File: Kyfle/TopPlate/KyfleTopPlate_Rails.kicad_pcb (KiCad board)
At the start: 2 copper layers, 164 x 146.3 mm, 28 parts, among them SW2 KEY_SWITCH, SW2 PRO MICRO

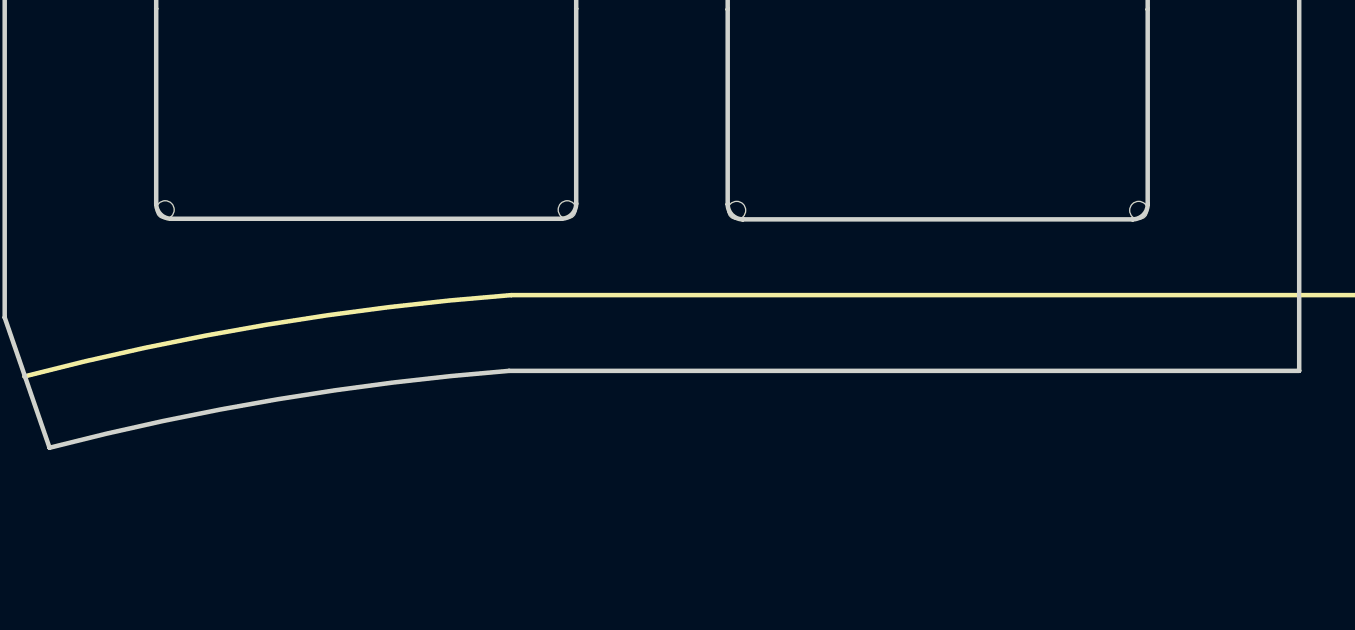
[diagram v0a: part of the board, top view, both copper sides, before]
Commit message: Found a solution to hold slightly better the middle "tongue" of board in the top plate with rails
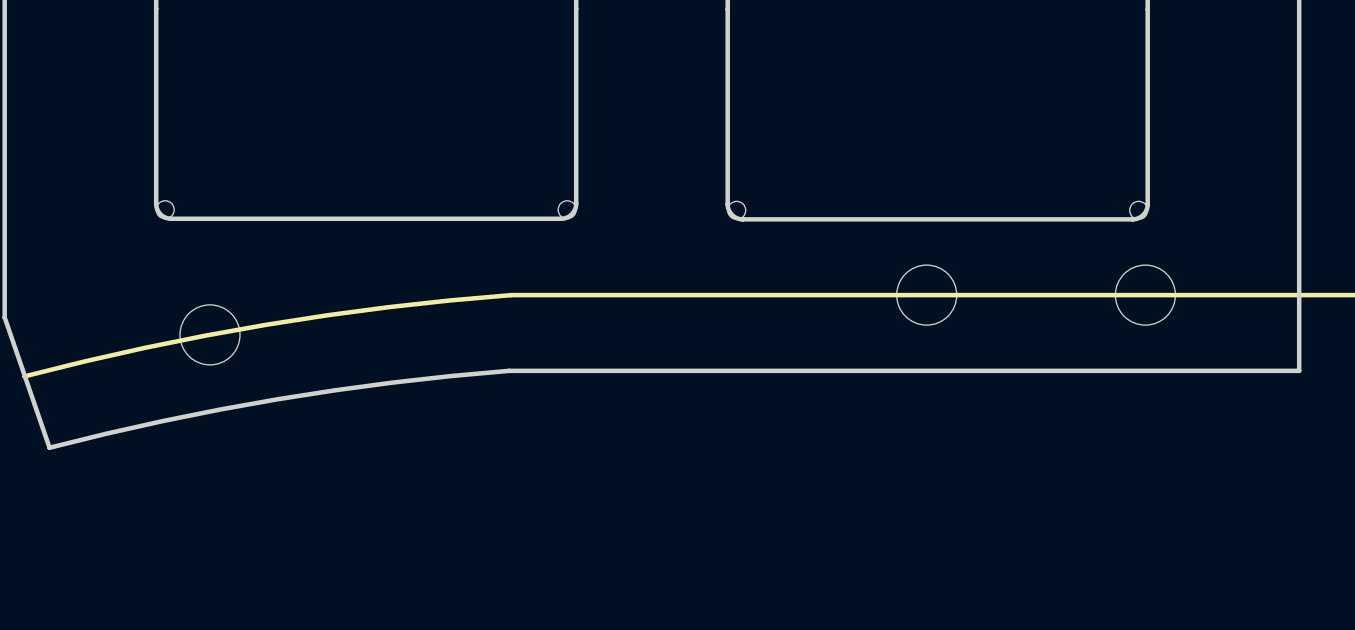
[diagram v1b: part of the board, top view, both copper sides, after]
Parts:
- removed the SW2 at (147.5, 119.4)
- added REF**: MountingHole_2.2mm_M2_ISO14580, Kyfle Footprints:M2_with_washer, F.Cu at (176.0, 108.6)
- added REF**: MountingHole_2.2mm_M2_ISO14580, Kyfle Footprints:M2_with_washer, F.Cu at (168.7, 108.6)
- added REF**: MountingHole_2.2mm_M2_ISO14580, Kyfle Footprints:M2_with_washer, F.Cu at (144.8, 109.9)
- added SW2: KEY_SWITCH, Kyfle Footprints:CherryMX_Kyfle_v1_TopPlate_1u_Rail_Helper, F.Cu at (147.5, 119.3)
- added SW2: KEY_SWITCH, Kyfle Footprints:CherryMX_Kyfle_v1_TopPlate_1u_Rail_Helper, F.Cu at (140.6, 120.9)

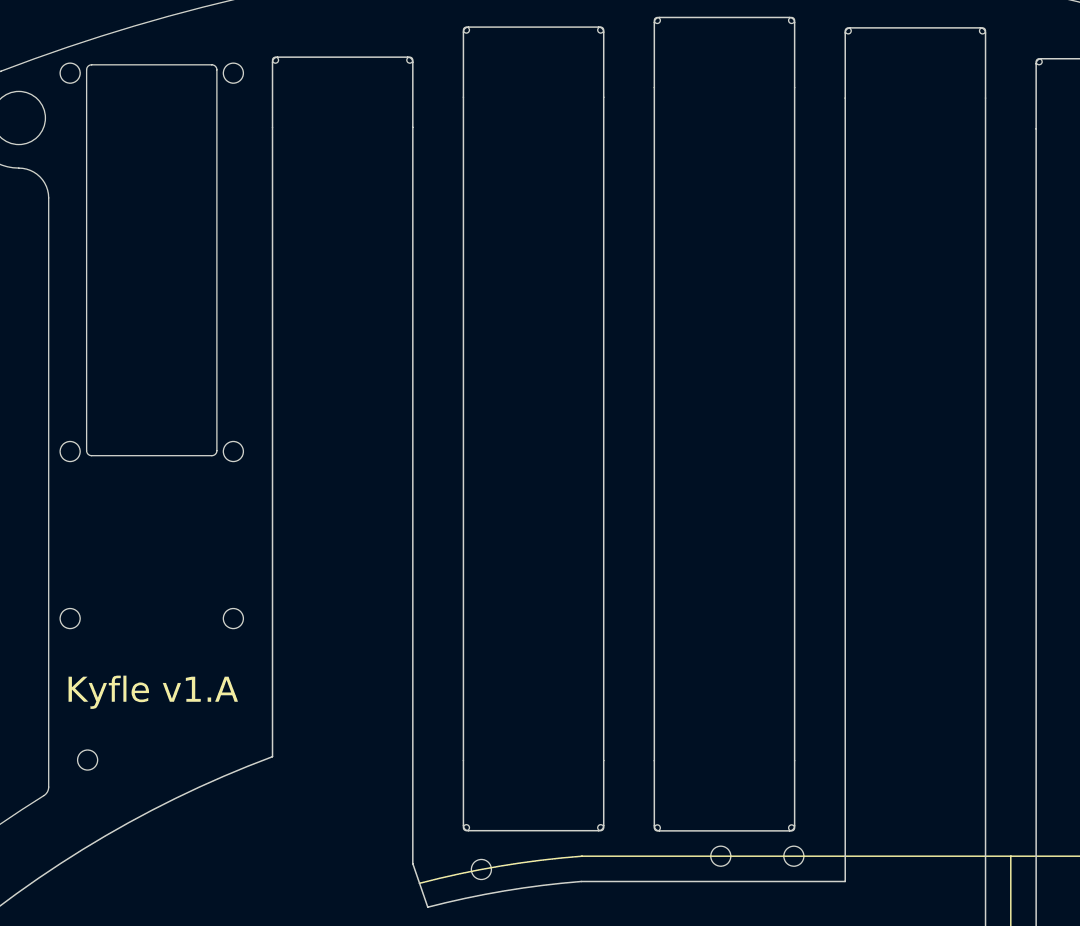
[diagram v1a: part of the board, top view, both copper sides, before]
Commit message: Plates: Received M2 and M5 hardware. It's bigger than specified...
- M5 screw head is ~9.5 instead of 8.7. Was colliding in the top left 
corner with M2 screw for pro micro board. So I shifted up pro micro 
board 0.3mm.
- M2 screw head is also larger than expected (3.8 instead of 3.2). But 
it is mostly fine as I was designing with 4-4.2mm clearance. Only 
exception was for screws supporting the middle bottom section of top 
plate with rails. Here it was colliding with switch housing. So, only 
solution is to use so called reduced slotted screws (DIN 920) as they 
have 2.8mm diameter head.
- Also added JLCPCB silk reference
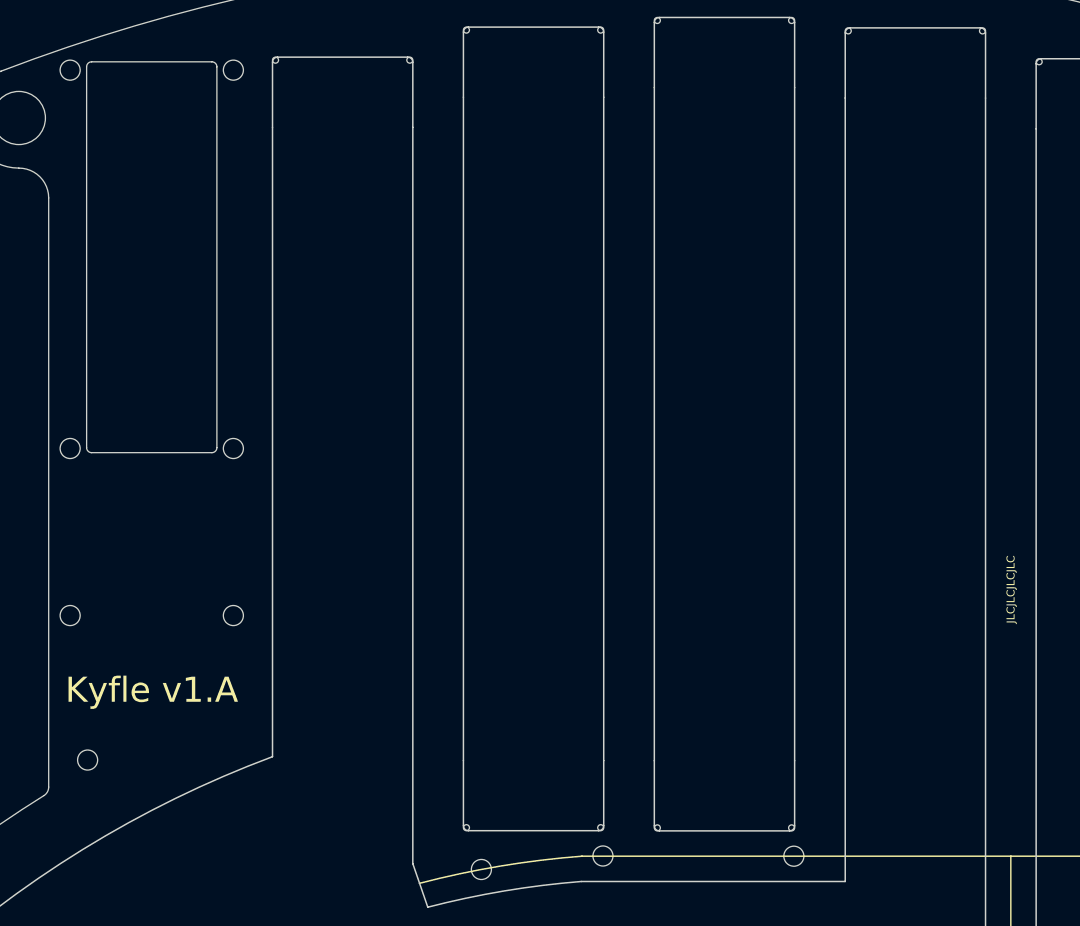
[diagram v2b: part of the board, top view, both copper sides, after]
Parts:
- added JLCJLCJLCJLC: JLCBCB_OrderNumber, Kyfle Footprints:JLCBCB_OrderNumber, F.Cu at (197.6, 82.0)
- moved REF** 11.8 mm to (156.9, 108.6)
- moved SW2 0.30 mm to (111.9, 58.4)
